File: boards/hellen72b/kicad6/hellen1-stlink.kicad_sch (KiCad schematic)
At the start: 8 parts

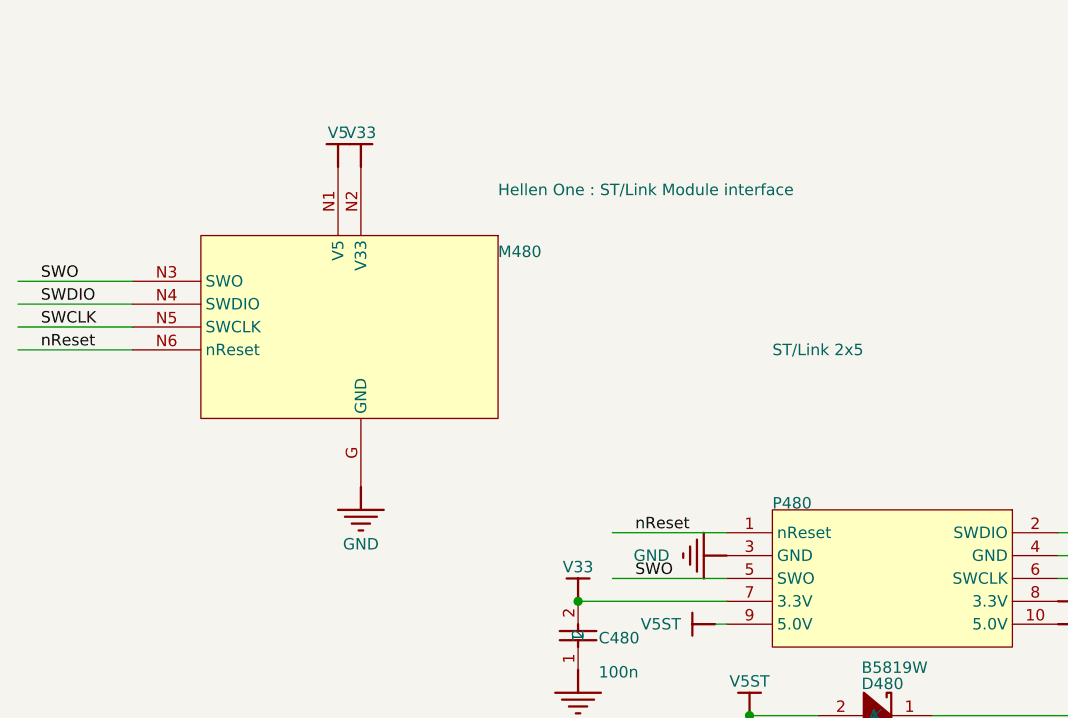
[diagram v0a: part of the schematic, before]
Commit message: update after refactoring can,lin,sd,stlink
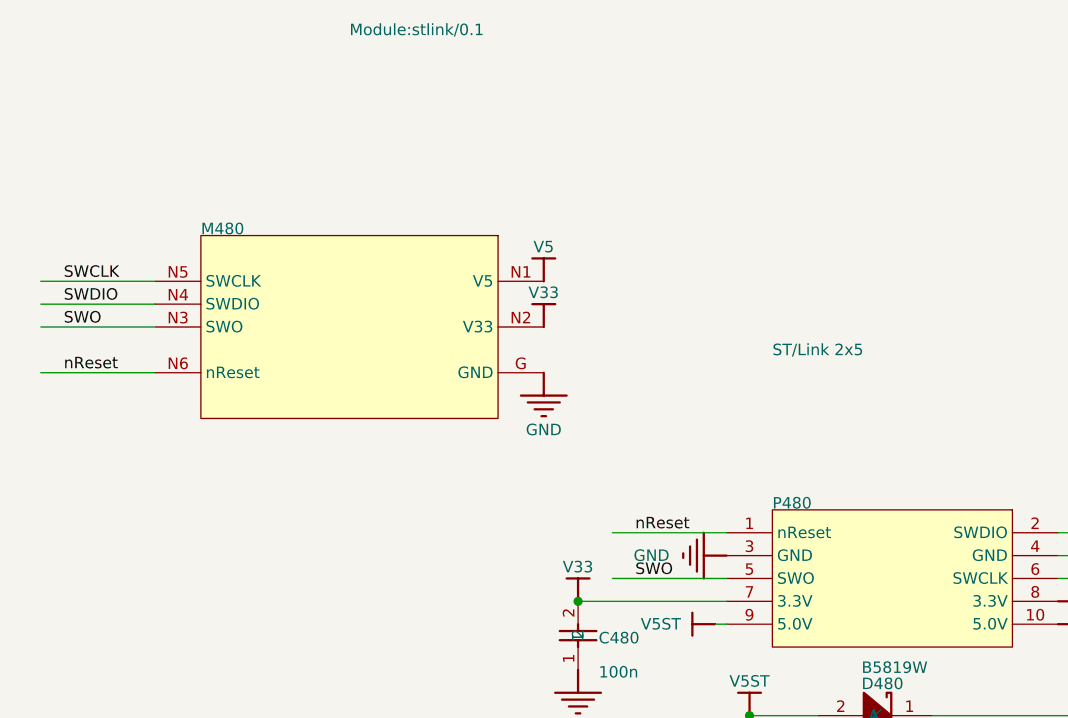
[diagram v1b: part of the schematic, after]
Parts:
- M480: Comment Hellen One : ST/Link Module interface -> Module:stlink/0.1
